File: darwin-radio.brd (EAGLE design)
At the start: 110 x 73 mm, 49 parts, among them J1 S1911-46R, Q2 NDS8434, U1 ATWINC, U2 INA219, U6 MCP7384X

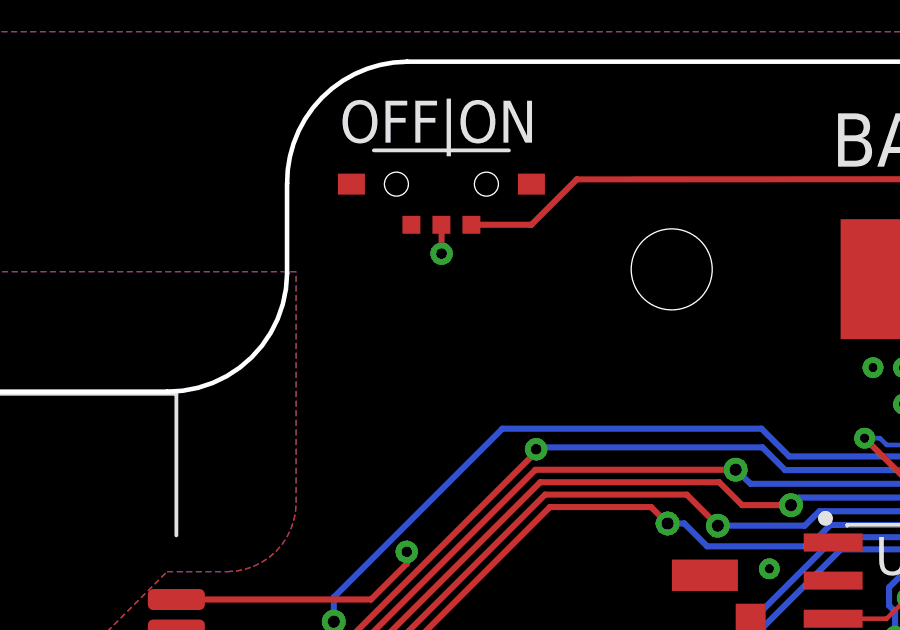
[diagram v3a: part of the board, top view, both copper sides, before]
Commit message: Added power switch headers.
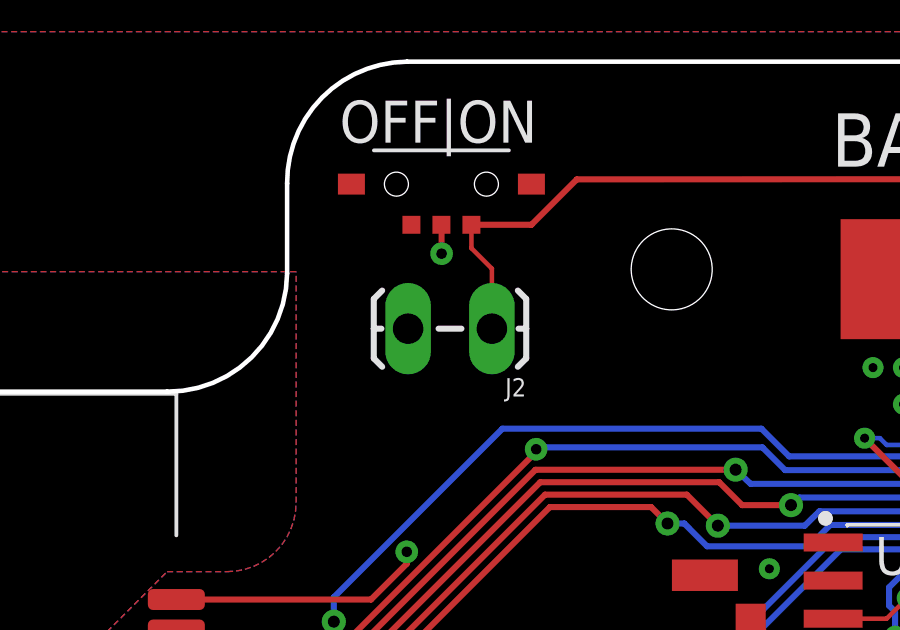
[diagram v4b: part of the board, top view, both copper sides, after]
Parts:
- added J2: (no value), SparkFun-Connectors:1X02_LOCK_LONGPADS
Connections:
- removed net N$8: R1.2, U$4.3, U$5.2
- new net PSWITCH: J2.1, R1.2, U$4.3, U$5.2
- net UNREG: now also J2.2
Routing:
- net PSWITCH: track 0.00 -> 69.0 mm
- net N$8: track 65.2 -> 0.00 mm
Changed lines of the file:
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@@
 <?xml version="1.0" encoding="utf-8"?>
 <!DOCTYPE eagle SYSTEM "eagle.dtd">
-<eagle version="9.5.0">
+<eagle version="9.5.2">
 <drawing>
 <settings>
@@
 <attribute name="SPICEPREFIX" value="C" x="60.5" y="46" size="1.778" layer="27" rot="R180" display="off"/>
 </element>
+<element name="J2" library="SparkFun-Connectors" library_urn="urn:adsk.eagle:library:513" package="1X02_LOCK_LONGPADS" package3d_urn="urn:adsk.eagle:package:38047/1" value="" x="28.7" y="64.1" smashed="yes" rot="R180">
+<attribute name="NAME" x="29.97" y="62.449" size="0.6096" layer="25" font="vector" ratio="20" rot="R180"/>
+<attribute name="VALUE" x="29.97" y="66.386" size="0.6096" layer="27" font="vector" ratio="20" rot="R180"/>
+</element>
 </elements>
 <signals>
@@
 <via x="70" y="40" extent="1-16" drill="0.3"/>
 <via x="70" y="42" extent="1-16" drill="0.3"/>
-<wire x1="9.6" y1="45.7" x2="10.4586" y2="46.4796" width="0" layer="19" extent="1-1"/>
-<wire x1="43.8912" y1="55.6768" x2="40.2019" y2="55.7022" width="0" layer="19" extent="1-1"/>
+<wire x1="40.2019" y1="55.7022" x2="43.8912" y2="55.6768" width="0" layer="19" extent="1-1"/>
+<wire x1="10.4586" y1="46.4796" x2="9.6" y2="45.7" width="0" layer="19" extent="1-1"/>
 </signal>
 <signal name="N$10">
@@
 <wire x1="73.3742" y1="53.1912" x2="73.4476" y2="53.1178" width="0.2032" layer="1"/>
 </signal>
-<signal name="N$8">
+<signal name="PSWITCH">
 <contactref element="U$5" pad="2"/>
 <contactref element="U$4" pad="3"/>
@@
 <wire x1="68.2752" y1="53.0352" x2="70.944" y2="53.0352" width="0.2032" layer="1"/>
 <wire x1="70.944" y1="53.0352" x2="71.1472" y2="53.2384" width="0.2032" layer="1"/>
+<contactref element="J2" pad="1"/>
+<wire x1="28.827" y1="64.1" x2="28.827" y2="66.1" width="0.1524" layer="1"/>
+<wire x1="28.827" y1="66.1" x2="28.1436" y2="66.7834" width="0.1524" layer="1"/>
+<wire x1="28.1436" y1="66.7834" x2="28.1436" y2="67.5626" width="0.1524" layer="1"/>
 </signal>
 <signal name="UNREG">
@@
 <wire x1="13.65804375" y1="24.1452" x2="13.415221875" y2="24.388021875" width="0.4064" layer="1"/>
 <via x="13.6144" y="24.384" extent="1-16" drill="0.3"/>
+<contactref element="J2" pad="2"/>
 <wire x1="13.6144" y1="24.384" x2="15.1316" y2="24.1452" width="0" layer="19" extent="1-1"/>
 </signal>

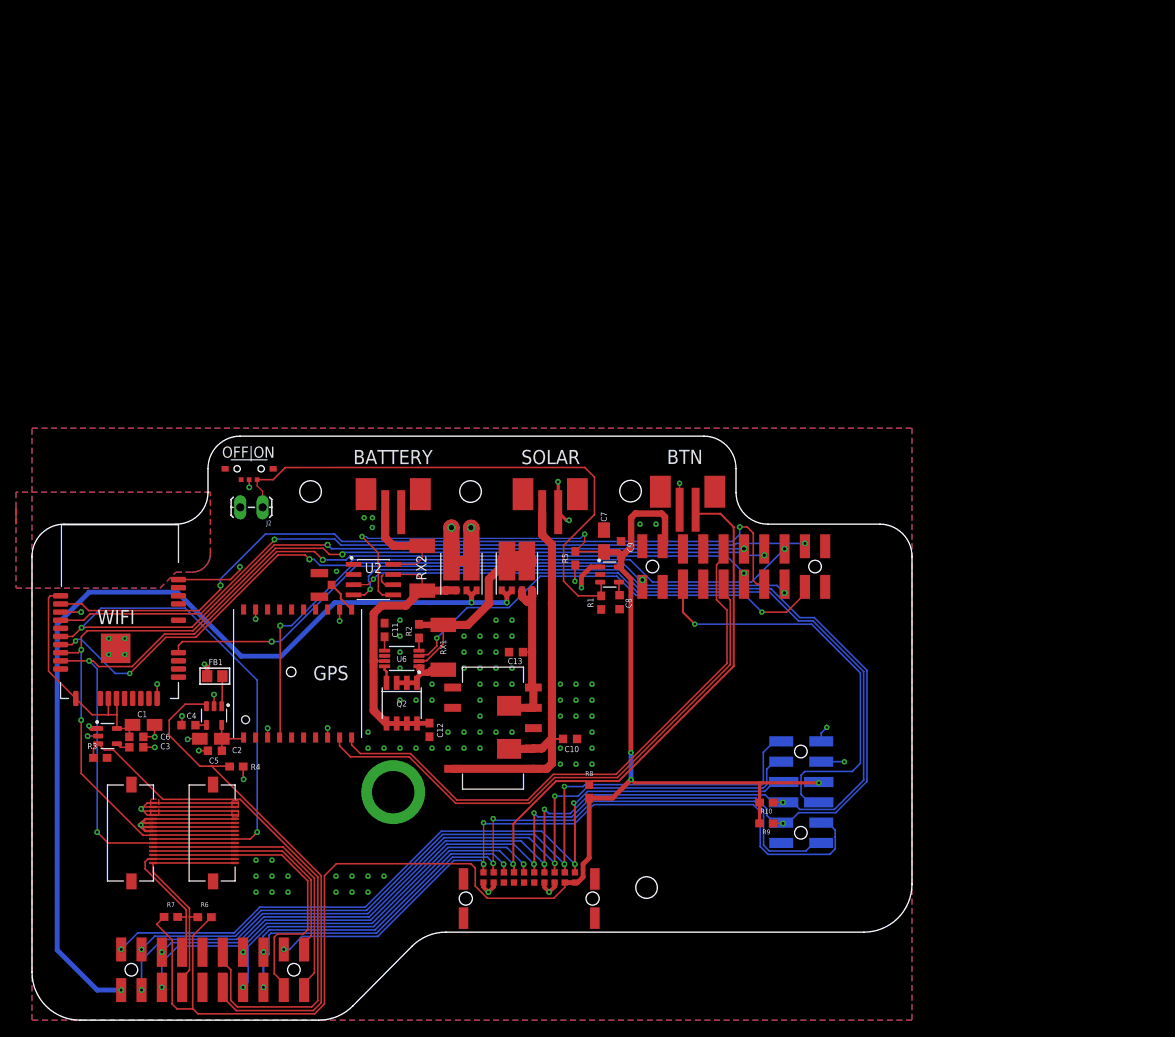
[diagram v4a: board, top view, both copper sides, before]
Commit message: Increased screw hole size and clearance diameter.
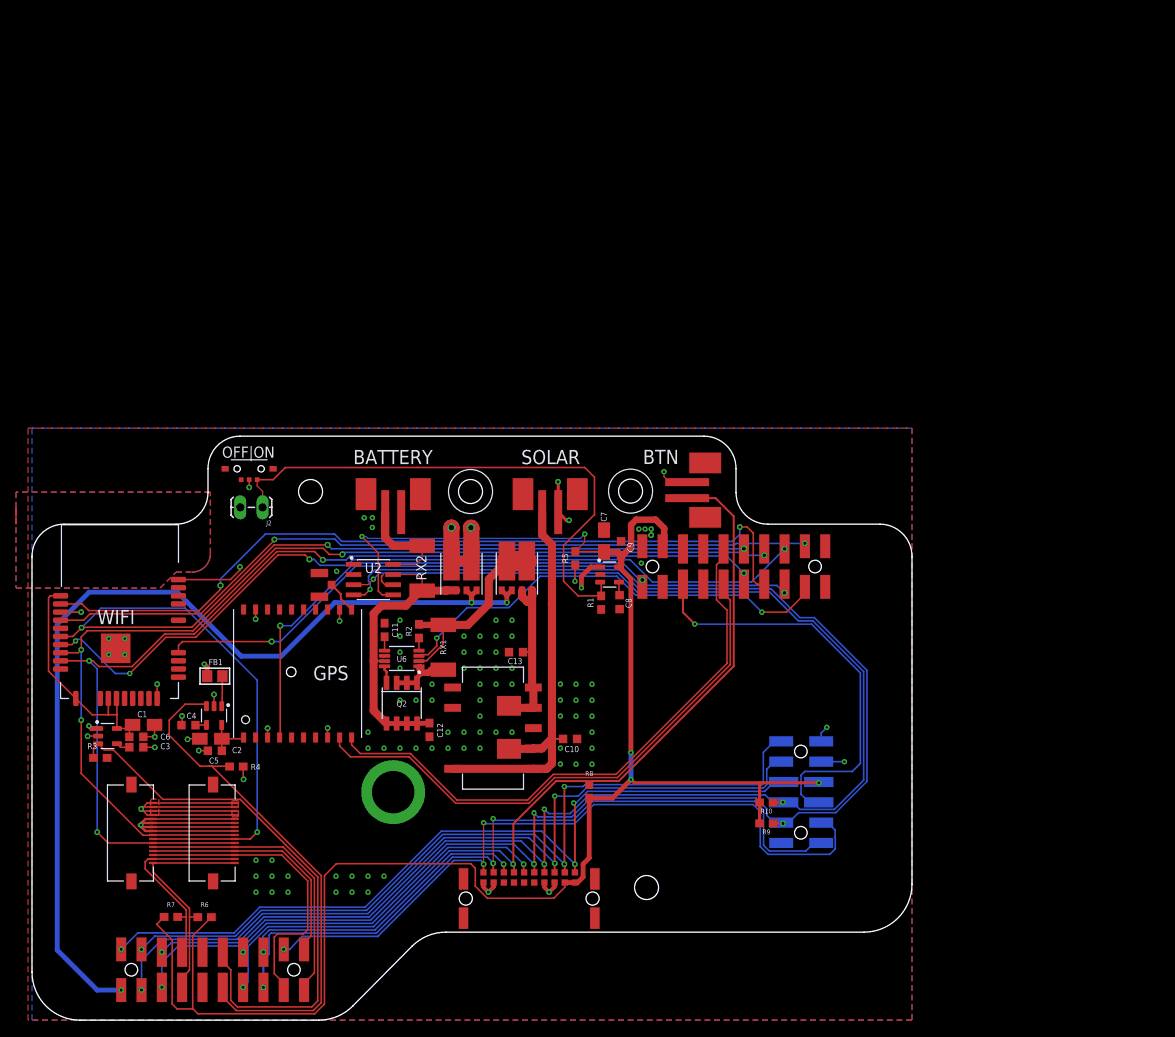
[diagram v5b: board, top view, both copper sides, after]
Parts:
- moved BTN-JST 1.73 mm to (82.9, 66.2), turned to 270 degrees
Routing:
- net XBTN: track 109.4 -> 111.8 mm
- net 3V3: track 232.1 -> 230.0 mm
- net GND: track 110.6 -> 111.1 mm, vias 101 -> 105
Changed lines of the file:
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@@
 <setting verticaltext="up"/>
 </settings>
-<grid distance="2" unitdist="mm" unit="mm" style="lines" multiple="1" display="yes" altdistance="0.1" altunitdist="mm" altunit="mm"/>
+<grid distance="1" unitdist="mm" unit="mm" style="lines" multiple="1" display="yes" altdistance="0.1" altunitdist="mm" altunit="mm"/>
 <layers>
 <layer number="1" name="Top" color="4" fill="1" visible="yes" active="yes"/>
@@
 <layer number="27" name="tValues" color="7" fill="1" visible="yes" active="yes"/>
 <layer number="28" name="bValues" color="7" fill="1" visible="yes" active="yes"/>
-<layer number="29" name="tStop" color="7" fill="3" visible="yes" active="yes"/>
-<layer number="30" name="bStop" color="7" fill="6" visible="yes" active="yes"/>
-<layer number="31" name="tCream" color="7" fill="4" visible="yes" active="yes"/>
-<layer number="32" name="bCream" color="7" fill="5" visible="yes" active="yes"/>
-<layer number="33" name="tFinish" color="6" fill="3" visible="yes" active="yes"/>
+<layer number="29" name="tStop" color="7" fill="3" visible="no" active="yes"/>
+<layer number="30" name="bStop" color="7" fill="6" visible="no" active="yes"/>
+<layer number="31" name="tCream" color="7" fill="4" visible="no" active="yes"/>
+<layer number="32" name="bCream" color="7" fill="5" visible="no" active="yes"/>
+<layer number="33" name="tFinish" color="6" fill="3" visible="no" active="yes"/>
 <layer number="34" name="bFinish" color="6" fill="6" visible="yes" active="yes"/>
 <layer number="35" name="tGlue" color="7" fill="4" visible="yes" active="yes"/>
@@
 <wire x1="18" y1="62" x2="4" y2="62" width="0.1524" layer="20"/>
 <wire x1="4" y1="62" x2="0" y2="57.9424" width="0.1524" layer="20" curve="90"/>
-<hole x="34.82" y="66.0764" drill="2.7"/>
-<hole x="54.816" y="66.0764" drill="2.7"/>
-<hole x="74.82" y="66.1264" drill="2.7"/>
+<hole x="34.82" y="66.0764" drill="3"/>
+<hole x="54.816" y="66.0764" drill="3"/>
+<hole x="74.82" y="66.1264" drill="3"/>
 <wire x1="0" y1="57.9424" x2="0" y2="6.0027" width="0.1524" layer="20"/>
 <wire x1="0" y1="6.0027" x2="5.9995" y2="0" width="0.1524" layer="20" curve="89.995225"/>
@@
 </polygon>
 <text x="23.75" y="70.3" size="1.4" layer="25" ratio="15">OFF|ON</text>
-<text x="83.85" y="71.3" size="1.778" layer="25" ratio="15" rot="R180">BTN</text>
-<hole x="76.82" y="16.5764" drill="2.7"/>
+<text x="80.85" y="71.3" size="1.778" layer="25" ratio="15" rot="R180">BTN</text>
+<hole x="76.82" y="16.5764" drill="3"/>
+<circle x="74.82" y="66.1264" radius="2.75" width="0.1397" layer="21"/>
+<circle x="54.816" y="66.0764" radius="2.75" width="0.1397" layer="21"/>
 </plain>
 <attributes>
@@
 </element>
 <element name="BACKPACK" library="Conservify" library_urn="urn:adsk.eagle:library:11839183" package="12PH" package3d_urn="urn:adsk.eagle:package:11839231/2" value="2X6-HEADERSDS" x="96.15" y="28.5" smashed="yes" rot="MR0"/>
-<element name="BTN-JST" library="Conservify" library_urn="urn:adsk.eagle:library:11839183" package="B2B-PH-SM4-TB" package3d_urn="urn:adsk.eagle:package:11839237/2" value="B2B-PH-SM4-TB" x="81.95" y="64.8" smashed="yes"/>
+<element name="BTN-JST" library="Conservify" library_urn="urn:adsk.eagle:library:11839183" package="B2B-PH-SM4-TB" package3d_urn="urn:adsk.eagle:package:11839237/2" value="B2B-PH-SM4-TB" x="82.9" y="66.25" smashed="yes" rot="R270"/>
 <element name="R8" library="SparkFun-Resistors" library_urn="urn:adsk.eagle:library:532" package="0603" package3d_urn="urn:adsk.eagle:package:39650/1" value="100k" x="69.65" y="28.6" smashed="yes" rot="R90">
 <attribute name="NAME" x="69.65" y="31.138" size="0.6096" layer="25" font="vector" ratio="20" rot="R180" align="bottom-center"/>
@@
 <wire x1="73.3466625" y1="29.886" x2="87.7136" y2="44.2529375" width="0.254" layer="1"/>
 <wire x1="60.1682" y1="24.54099375" x2="65.50900625" y2="29.8818" width="0.254" layer="1"/>
-<wire x1="87.7136" y1="61.6364" x2="87.7136" y2="44.2529375" width="0.254" layer="1"/>
 <contactref element="BTN-JST" pad="-"/>
 <contactref element="R8" pad="2"/>
@@
 <wire x1="73.3466625" y1="29.886" x2="70.086" y2="29.886" width="0.254" layer="1"/>
 <wire x1="69.65" y1="29.45" x2="70.086" y2="29.886" width="0.254" layer="1"/>
-<wire x1="86.05" y1="63.3" x2="83.45" y2="63.3" width="0.254" layer="1"/>
-<wire x1="82.95" y1="63.8" x2="83.45" y2="63.3" width="0.1524" layer="1"/>
-<wire x1="86.05" y1="63.3" x2="87.7136" y2="61.6364" width="0.254" layer="1"/>
 <wire x1="58.4436" y1="21.1836" x2="60.15" y2="19.5" width="0.2032" layer="16"/>
 <wire x1="27.0256" y1="4.7356" x2="26.39" y2="4.1" width="0.2032" layer="16"/>
@@
 <wire x1="52.184425" y1="21.1836" x2="58.4436" y2="21.1836" width="0.2032" layer="16"/>
 <wire x1="29.4929" y1="11.6872" x2="27.0256" y2="9.2199" width="0.2032" layer="16"/>
+<wire x1="87.7136" y1="62.98153125" x2="85.44513125" y2="65.25" width="0.254" layer="1"/>
+<wire x1="85.44513125" y1="65.25" x2="81.9" y2="65.25" width="0.254" layer="1"/>
+<wire x1="87.7136" y1="44.2529375" x2="87.7136" y2="62.98153125" width="0.254" layer="1"/>
 </signal>
 <signal name="MOD_G5">
@@
 <wire x1="74.893" y1="59.1644" x2="73.8364" y2="58.1078" width="0.8128" layer="1"/>
 <wire x1="73.6364" y1="58.1078" x2="73.8364" y2="58.1078" width="0.8128" layer="1"/>
-<wire x1="74.893" y1="59.1644" x2="74.893" y2="62.8002625" width="0.8128" layer="1"/>
-<wire x1="74.893" y1="62.8002625" x2="75.4151375" y2="63.3224" width="0.8128" layer="1"/>
-<wire x1="75.4151375" y1="63.3224" x2="78.7096" y2="63.3224" width="0.8128" layer="1"/>
-<wire x1="78.7096" y1="63.3224" x2="79.13" y2="62.902" width="0.8128" layer="1"/>
-<wire x1="79.13" y1="62.902" x2="79.13" y2="59.54" width="0.8128" layer="1"/>
-<wire x1="79.13" y1="59.54" x2="78.83" y2="59.24" width="0.8128" layer="1"/>
+<wire x1="74.893" y1="59.1644" x2="74.893" y2="61.939" width="0.8128" layer="1"/>
+<wire x1="74.893" y1="61.939" x2="75.5144" y2="62.5604" width="0.8128" layer="1"/>
+<wire x1="75.5144" y1="62.5604" x2="77.9524" y2="62.5604" width="0.8128" layer="1"/>
+<wire x1="77.9524" y1="62.5604" x2="79.03" y2="61.4828" width="0.8128" layer="1"/>
+<wire x1="79.03" y1="61.4828" x2="79.03" y2="59.44" width="0.8128" layer="1"/>
+<wire x1="79.03" y1="59.44" x2="78.83" y2="59.24" width="0.8128" layer="1"/>
 <wire x1="73.3742" y1="56.652" x2="74.859378125" y2="55.166821875" width="0.6096" layer="1"/>
 <wire x1="74.859378125" y1="55.166821875" x2="74.859378125" y2="33.446221875" width="0.6096" layer="1"/>
@@
 <via x="101.55" y="32.3" extent="1-16" drill="0.3"/>
 <contactref element="BTN-JST" pad="+"/>
-<wire x1="80.95" y1="63.8" x2="80.95" y2="67.1" width="0.1524" layer="1"/>
-<via x="80.95" y="67.1" extent="1-16" drill="0.3"/>
+<wire x1="81.9" y1="67.25" x2="79.7" y2="67.25" width="0.1524" layer="1"/>
+<wire x1="79" y1="68.55" x2="79" y2="67.95" width="0.1524" layer="1"/>
+<wire x1="79.7" y1="67.25" x2="79" y2="67.95" width="0.1524" layer="1"/>
+<via x="79" y="68.55" extent="1-16" drill="0.3"/>
 <contactref element="REG1" pad="P$3"/>
 <contactref element="REG1" pad="P$7"/>
@@
 </polygon>
 <polygon width="0.4064" layer="1">
-<vertex x="0" y="0"/>
-<vertex x="0" y="74"/>
+<vertex x="-0.5" y="0"/>
+<vertex x="-0.5" y="74"/>
 <vertex x="110" y="74"/>
 <vertex x="110" y="0"/>
@@
 <vertex x="-2" y="62"/>
 </polygon>
-<via x="76" y="62" extent="1-16" drill="0.3"/>
-<via x="78" y="62" extent="1-16" drill="0.3"/>
+<via x="76.6284" y="61.3904" extent="1-16" drill="0.3"/>
 <wire x1="45.1421" y1="54.4322" x2="44.1262" y2="54.4322" width="0.2032" layer="1"/>
 <wire x1="44.1262" y1="54.4322" x2="43.6944" y2="54.864" width="0.2032" layer="1"/>
@@
 <via x="70" y="40" extent="1-16" drill="0.3"/>
 <via x="70" y="42" extent="1-16" drill="0.3"/>
+<via x="77.3904" y="61.3904" extent="1-16" drill="0.3"/>
+<via x="77.3904" y="60.6284" extent="1-16" drill="0.3"/>
+<via x="77.3904" y="60.6284" extent="1-16" drill="0.3"/>
+<via x="75.8664" y="61.3904" extent="1-16" drill="0.3"/>
+<via x="76.1712" y="57.1232" extent="1-16" drill="0.3"/>
 <wire x1="40.2019" y1="55.7022" x2="43.8912" y2="55.6768" width="0" layer="19" extent="1-1"/>
 <wire x1="10.4586" y1="46.4796" x2="9.6" y2="45.7" width="0" layer="19" extent="1-1"/>
